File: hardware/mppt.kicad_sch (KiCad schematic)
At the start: 40 parts, among them J1 Conn_01x04_Pin, Q1 BC817, Q2 NTR4171PT1G, U1 INA226, U2 INA226

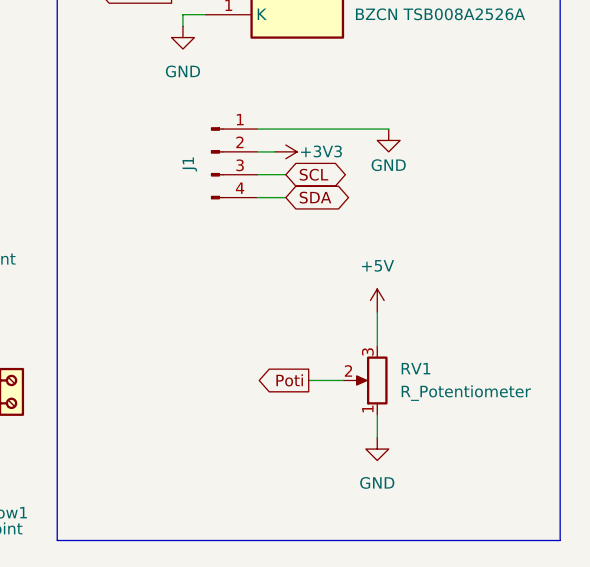
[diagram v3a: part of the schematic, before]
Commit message: Connected 3.3V instead of 5V to slider poti. This makes the full range available for esp32 and avoids damage to the board
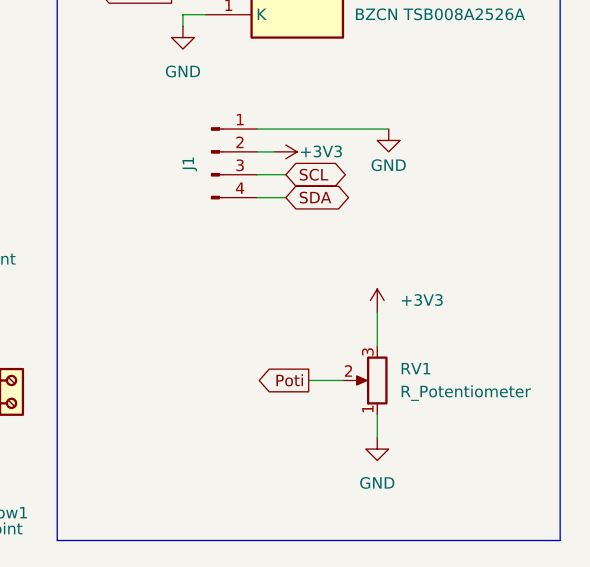
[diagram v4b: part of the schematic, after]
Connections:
- net +3V3: now also RV1.3
- net +5V: no longer RV1.3
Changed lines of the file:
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@@
 		)
 		(instances
-			(project "Untitled"
+			(project "mppt"
 				(path "/640b6820-0858-468d-a0f2-29dab814e1ab"
 					(reference "#PWR02")
@@
 		)
 		(instances
-			(project ""
+			(project "mppt"
 				(path "/640b6820-0858-468d-a0f2-29dab814e1ab"
 					(reference "#PWR01")
@@
 		)
 		(instances
-			(project "Untitled"
+			(project "mppt"
 				(path "/640b6820-0858-468d-a0f2-29dab814e1ab"
 					(reference "#PWR010")
@@
 		)
 		(instances
-			(project "Untitled"
+			(project "mppt"
 				(path "/640b6820-0858-468d-a0f2-29dab814e1ab"
 					(reference "VOUT2")
@@
 		)
 		(instances
-			(project "Untitled"
+			(project "mppt"
 				(path "/640b6820-0858-468d-a0f2-29dab814e1ab"
 					(reference "C4")
@@
 		)
 		(instances
-			(project "Untitled"
+			(project "mppt"
 				(path "/640b6820-0858-468d-a0f2-29dab814e1ab"
 					(reference "Q1")
@@
 		)
 		(instances
-			(project ""
+			(project "mppt"
 				(path "/640b6820-0858-468d-a0f2-29dab814e1ab"
 					(reference "Rshunt1")
@@
 		)
 		(instances
-			(project "Untitled"
+			(project "mppt"
 				(path "/640b6820-0858-468d-a0f2-29dab814e1ab"
 					(reference "VOUTlow1")
@@
 		)
 		(instances
-			(project "Untitled"
+			(project "mppt"
 				(path "/640b6820-0858-468d-a0f2-29dab814e1ab"
 					(reference "H4")
@@
 		)
 		(instances
-			(project "Untitled"
+			(project "mppt"
 				(path "/640b6820-0858-468d-a0f2-29dab814e1ab"
 					(reference "R3")
@@
 		)
 		(instances
-			(project "Untitled"
+			(project "mppt"
 				(path "/640b6820-0858-468d-a0f2-29dab814e1ab"
 					(reference "VIN1")
@@
 		)
 		(instances
-			(project ""
+			(project "mppt"
 				(path "/640b6820-0858-468d-a0f2-29dab814e1ab"
 					(reference "R2")
@@
 		)
 		(instances
-			(project "Untitled"
+			(project "mppt"
 				(path "/640b6820-0858-468d-a0f2-29dab814e1ab"
 					(reference "C5")
@@
 		)
 		(instances
-			(project ""
+			(project "mppt"
 				(path "/640b6820-0858-468d-a0f2-29dab814e1ab"
 					(reference "S1")
@@
 		)
 		(instances
-			(project "Untitled"
+			(project "mppt"
 				(path "/640b6820-0858-468d-a0f2-29dab814e1ab"
 					(reference "R4")
@@
 		)
 		(instances
-			(project ""
+			(project "mppt"
 				(path "/640b6820-0858-468d-a0f2-29dab814e1ab"
 					(reference "C2")
@@
 		)
 		(instances
-			(project ""
+			(project "mppt"
 				(path "/640b6820-0858-468d-a0f2-29dab814e1ab"
 					(reference "J1")
@@
 		)
 		(instances
-			(project "Untitled"
+			(project "mppt"
 				(path "/640b6820-0858-468d-a0f2-29dab814e1ab"
 					(reference "#PWR012")
@@
 		)
 		(instances
-			(project "Untitled"
+			(project "mppt"
 				(path "/640b6820-0858-468d-a0f2-29dab814e1ab"
 					(reference "R5")
@@
 		)
 		(instances
-			(project ""
+			(project "mppt"
 				(path "/640b6820-0858-468d-a0f2-29dab814e1ab"
 					(reference "RV1")
@@
 		)
 		(instances
-			(project "Untitled"
+			(project "mppt"
 				(path "/640b6820-0858-468d-a0f2-29dab814e1ab"
 					(reference "H3")
@@
 		)
 		(instances
-			(project "Untitled"
+			(project "mppt"
 				(path "/640b6820-0858-468d-a0f2-29dab814e1ab"
 					(reference "H2")
@@
 			)
 		)
-		(property "Value" "+5V"
-			(at 262.89 62.23 0)
+		(property "Value" "+3V3"
+			(at 265.43 66.0399 0)
 			(effects
 				(font
 					(size 1.27 1.27)
 				)
+				(justify left)
 			)
 		)
@@
 		)
 		(instances
-			(project "Untitled"
+			(project "mppt"
 				(path "/640b6820-0858-468d-a0f2-29dab814e1ab"
 					(reference "#PWR03")
@@
 		)
 		(instances
-			(project ""
+			(project "mppt"
 				(path "/640b6820-0858-468d-a0f2-29dab814e1ab"
 					(reference "Arduino1")
@@
 		)
 		(instances
-			(project "Untitled"
+			(project "mppt"
 				(path "/640b6820-0858-468d-a0f2-29dab814e1ab"
 					(reference "C1")
@@
 		)
 		(instances
-			(project ""
+			(project "mppt"
 				(path "/640b6820-0858-468d-a0f2-29dab814e1ab"
 					(reference "H1")
@@
 		)
 		(instances
-			(project "Untitled"
+			(project "mppt"
 				(path "/640b6820-0858-468d-a0f2-29dab814e1ab"
 					(reference "#PWR011")
@@
 		)
 		(instances
-			(project "Untitled"
+			(project "mppt"
 				(path "/640b6820-0858-468d-a0f2-29dab814e1ab"
 					(reference "#PWR013")
@@
 		)
 		(instances
-			(project "Untitled"
+			(project "mppt"
 				(path "/640b6820-0858-468d-a0f2-29dab814e1ab"
 					(reference "Q2")
@@
 		)
 		(instances
-			(project "Untitled"
+			(project "mppt"
 				(path "/640b6820-0858-468d-a0f2-29dab814e1ab"
 					(reference "#PWR06")
@@
 		)
 		(instances
-			(project ""
+			(project "mppt"
 				(path "/640b6820-0858-468d-a0f2-29dab814e1ab"
 					(reference "D1")
@@
 		)
 		(instances
-			(project ""
+			(project "mppt"
 				(path "/640b6820-0858-468d-a0f2-29dab814e1ab"
 					(reference "Panel_IN1")
@@
 		)
 		(instances
-			(project "Untitled"
+			(project "mppt"
 				(path "/640b6820-0858-468d-a0f2-29dab814e1ab"
 					(reference "#PWR05")
@@
 		)
 		(instances
-			(project "Untitled"
+			(project "mppt"
 				(path "/640b6820-0858-468d-a0f2-29dab814e1ab"
 					(reference "#PWR07")
@@
 		)
 		(instances
-			(project "Untitled"
+			(project "mppt"
 				(path "/640b6820-0858-468d-a0f2-29dab814e1ab"
 					(reference "C6")
@@
 		)
 		(instances
-			(project ""
+			(project "mppt"
 				(path "/640b6820-0858-468d-a0f2-29dab814e1ab"
 					(reference "U1")
@@
 		)
 		(instances
-			(project "Untitled"
+			(project "mppt"
 				(path "/640b6820-0858-468d-a0f2-29dab814e1ab"
 					(reference "#PWR04")
@@
 		)
 		(instances
-			(project ""
+			(project "mppt"
 				(path "/640b6820-0858-468d-a0f2-29dab814e1ab"
 					(reference "L1")
@@
 		)
 		(instances
-			(project ""
+			(project "mppt"
 				(path "/640b6820-0858-468d-a0f2-29dab814e1ab"
 					(reference "R1")
@@
 		)
 		(instances
-			(project "Untitled"
+			(project "mppt"
 				(path "/640b6820-0858-468d-a0f2-29dab814e1ab"
 					(reference "VOUT1")
@@
 		)
 		(instances
-			(project ""
+			(project "mppt"
 				(path "/640b6820-0858-468d-a0f2-29dab814e1ab"
 					(reference "C3")
@@
 		)
 		(instances
-			(project ""
+			(project "mppt"
 				(path "/640b6820-0858-468d-a0f2-29dab814e1ab"
 					(reference "R6")
@@
 		)
 		(instances
-			(project "Untitled"
+			(project "mppt"
 				(path "/640b6820-0858-468d-a0f2-29dab814e1ab"
 					(reference "R_Gate1")
